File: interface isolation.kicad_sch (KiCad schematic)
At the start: 27 parts, among them J1 Conn_01x09_Socket, J2 Conn_01x02, Q1 Q_NPN_BCE, Q2 Q_NPN_BCE, Q3 Q_NPN_BCE, Q4 Q_NPN_BCE, U1 PC817, U2 PC817, U3 PC817, U4 PC817

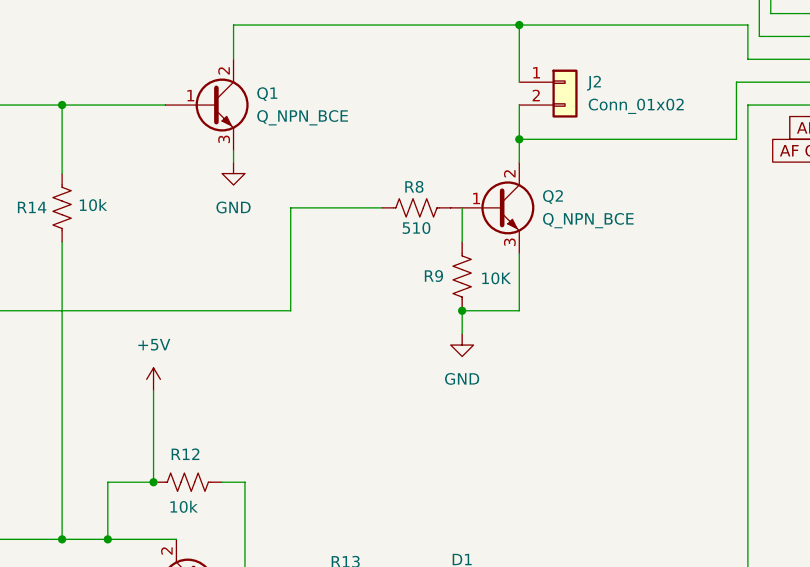
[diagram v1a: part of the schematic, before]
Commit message: Assign footprints to devices
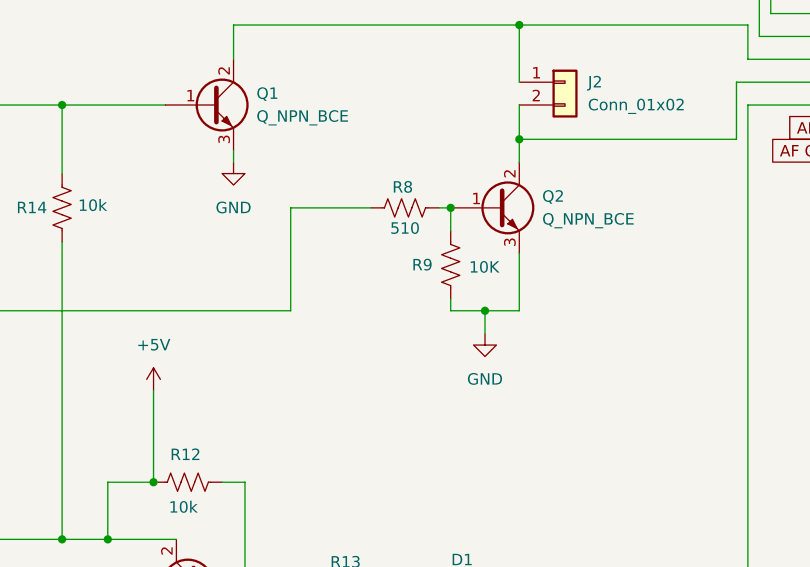
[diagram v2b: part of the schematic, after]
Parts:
- C6: footprint (none) -> Capacitor_SMD:C_0201_0603Metric
- D1, D2: footprint Diode_THT:D_DO-35_SOD27_P7.62mm_Horizontal -> Diode_SMD:D_0603_1608Metric
- J1: footprint (none) -> Connector_Dsub:DSUB-9_Male_EdgeMount_P2.77mm
- J2: footprint (none) -> Connector_PinHeader_1.00mm:PinHeader_1x02_P1.00mm_Vertical
- Q1, Q2, Q3, Q4: footprint (none) -> Package_TO_SOT_SMD:SOT-23-3
- R1, R10, R11, R12, R13, R14, R2, R3, R4, R5, R6, R7, R8, R9: footprint (none) -> Resistor_SMD:R_0201_0603Metric
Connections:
- net at R9.2: now also Q2.1 (B), R8.2
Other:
- moved on the sheet: R8, R9
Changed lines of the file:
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@@
 	)
 	(junction
-		(at 137.16 142.24)
+		(at 171.45 100.33)
 		(diameter 0)
 		(color 0 0 0 0)
 	)
 	(junction
-		(at 168.91 100.33)
+		(at 137.16 142.24)
 		(diameter 0)
 		(color 0 0 0 0)
@@
 	)
 	(junction
+		(at 167.64 88.9)
+		(diameter 0)
+		(color 0 0 0 0)
+	)
+	(junction
 		(at 144.78 130.81)
 		(diameter 0)
@@
 	(wire
 		(pts
-			(xy 149.86 88.9) (xy 160.02 88.9)
+			(xy 149.86 88.9) (xy 158.75 88.9)
 		)
 		(stroke
@@
 	(wire
 		(pts
-			(xy 168.91 100.33) (xy 168.91 102.87)
+			(xy 171.45 100.33) (xy 171.45 102.87)
 		)
 		(stroke
@@
 	(wire
 		(pts
+			(xy 167.64 99.06) (xy 167.64 100.33)
+		)
+		(stroke
+			(width 0)
+			(type default)
+		)
+	)
+	(wire
+		(pts
 			(xy 107.95 52.07) (xy 101.6 52.07)
 		)
@@
 	(wire
 		(pts
+			(xy 167.64 100.33) (xy 171.45 100.33)
+		)
+		(stroke
+			(width 0)
+			(type default)
+		)
+	)
+	(wire
+		(pts
 			(xy 199.39 74.93) (xy 213.36 74.93)
 		)
@@
 	(wire
 		(pts
-			(xy 175.26 100.33) (xy 168.91 100.33)
+			(xy 175.26 100.33) (xy 171.45 100.33)
 		)
 		(stroke
@@
 	(wire
 		(pts
+			(xy 166.37 88.9) (xy 167.64 88.9)
+		)
+		(stroke
+			(width 0)
+			(type default)
+		)
+	)
+	(wire
+		(pts
 			(xy 105.41 147.32) (xy 105.41 152.4)
 		)
@@
 	(wire
 		(pts
-			(xy 168.91 88.9) (xy 168.91 92.71)
+			(xy 167.64 88.9) (xy 167.64 91.44)
 		)
 		(stroke
@@
 	(symbol
 		(lib_id "Device:R_US")
-		(at 168.91 96.52 180)
+		(at 167.64 95.25 180)
 		(unit 1)
 		(exclude_from_sim no)
@@
 		(dnp no)
 		(property "Reference" "R9"
-			(at 164.592 96.52 0)
+			(at 163.322 95.25 0)
 			(effects
 				(font
@@
 		)
 		(property "Value" "10K"
-			(at 170.942 96.774 0)
+			(at 169.672 95.504 0)
 			(effects
 				(font
@@
 			)
 		)
-		(property "Footprint" ""
-			(at 167.894 96.266 90)
+		(property "Footprint" "Resistor_SMD:R_0201_0603Metric"
+			(at 166.624 94.996 90)
 			(effects
 				(font
@@
 		)
 		(property "Datasheet" "~"
-			(at 168.91 96.52 0)
+			(at 167.64 95.25 0)
 			(effects
 				(font
@@
 		)
 		(property "Description" "Resistor, US symbol"
-			(at 168.91 96.52 0)
+			(at 167.64 95.25 0)
 			(effects
 				(font
@@
 			)
 		)
-		(property "Footprint" ""
+		(property "Footprint" "Resistor_SMD:R_0201_0603Metric"
 			(at 123.444 88.646 90)
 			(effects
@@
 	(symbol
 		(lib_id "Device:R_US")
-		(at 163.83 88.9 90)
+		(at 162.56 88.9 90)
 		(unit 1)
 		(exclude_from_sim no)
@@
 		(dnp no)
 		(property "Reference" "R8"
-			(at 163.576 86.614 90)
+			(at 162.306 86.614 90)
 			(effects
 				(font
@@
 		)
 		(property "Value" "510"
-			(at 163.83 91.186 90)
+			(at 162.56 91.186 90)
 			(effects
 				(font
@@
 			)
 		)
-		(property "Footprint" ""
-			(at 164.084 87.884 90)
+		(property "Footprint" "Resistor_SMD:R_0201_0603Metric"
+			(at 162.814 87.884 90)
 			(effects
 				(font
@@
 		)
 		(property "Datasheet" "~"
-			(at 163.83 88.9 0)
+			(at 162.56 88.9 0)
 			(effects
 				(font
@@
 		)
 		(property "Description" "Resistor, US symbol"
-			(at 163.83 88.9 0)
+			(at 162.56 88.9 0)
 			(effects
 				(font
@@
 			)
 		)
-		(property "Footprint" ""
+		(property "Footprint" "Connector_Dsub:DSUB-9_Male_EdgeMount_P2.77mm"
 			(at 218.44 77.47 0)
 			(effects
@@
 			)
 		)
-		(property "Footprint" ""
+		(property "Footprint" "Resistor_SMD:R_0201_0603Metric"
 			(at 75.184 76.454 90)
 			(effects
@@
 			)
 		)
-		(property "Footprint" ""
+		(property "Footprint" "Resistor_SMD:R_0201_0603Metric"
 			(at 171.704 51.054 90)
 			(effects
@@
 			)
 		)
-		(property "Footprint" ""
+		(property "Footprint" "Resistor_SMD:R_0201_0603Metric"
 			(at 136.144 145.796 90)
 			(effects
@@
 			)
 		)
-		(property "Footprint" ""
+		(property "Footprint" "Resistor_SMD:R_0201_0603Metric"
 			(at 138.684 118.364 90)
 			(effects
@@
 			)
 		)
-		(property "Footprint" ""
+		(property "Footprint" "Resistor_SMD:R_0201_0603Metric"
 			(at 106.934 64.516 90)
 			(effects
@@
 			)
 		)
-		(property "Footprint" ""
+		(property "Footprint" "Resistor_SMD:R_0201_0603Metric"
 			(at 156.464 129.794 90)
 			(effects
@@
 			)
 		)
-		(property "Footprint" ""
+		(property "Footprint" "Connector_PinHeader_1.00mm:PinHeader_1x02_P1.00mm_Vertical"
 			(at 180.34 74.93 0)
 			(effects
@@
 			)
 		)
-		(property "Footprint" "Diode_THT:D_DO-35_SOD27_P7.62mm_Horizontal"
+		(property "Footprint" "Diode_SMD:D_0603_1608Metric"
 			(at 168.91 130.81 0)
 			(effects
@@
 			)
 		)
-		(property "Footprint" ""
+		(property "Footprint" "Capacitor_SMD:C_0201_0603Metric"
 			(at 117.8052 139.7 0)
 			(effects
@@
 			)
 		)
-		(property "Footprint" ""
+		(property "Footprint" "Package_TO_SOT_SMD:SOT-23-3"
 			(at 177.8 86.36 0)
 			(effects
@@
 			)
 		)
-		(property "Footprint" ""
+		(property "Footprint" "Resistor_SMD:R_0201_0603Metric"
 			(at 73.914 99.314 90)
 			(effects
@@
 			)
 		)
-		(property "Footprint" ""
+		(property "Footprint" "Package_TO_SOT_SMD:SOT-23-3"
 			(at 134.62 128.27 0)
 			(effects
@@
 			)
 		)
-		(property "Footprint" ""
+		(property "Footprint" "Resistor_SMD:R_0201_0603Metric"
 			(at 72.136 138.684 90)
 			(effects
@@
 			)
 		)
-		(property "Footprint" ""
+		(property "Footprint" "Package_TO_SOT_SMD:SOT-23-3"
 			(at 146.05 74.93 0)
 			(effects
@@
 			)
 		)
-		(property "Footprint" ""
+		(property "Footprint" "Resistor_SMD:R_0201_0603Metric"
 			(at 152.654 54.864 90)
 			(effects
@@
 	(symbol
 		(lib_id "power:GND")
-		(at 168.91 102.87 0)
+		(at 171.45 102.87 0)
 		(unit 1)
 		(exclude_from_sim no)
@@
 		(fields_autoplaced yes)
 		(property "Reference" "#PWR020"
-			(at 168.91 109.22 0)
+			(at 171.45 109.22 0)
 			(effects
 				(font
@@
 		)
 		(property "Value" "GND"
-			(at 168.91 107.95 0)
+			(at 171.45 107.95 0)
 			(effects
 				(font
@@
 		)
 		(property "Footprint" ""
-			(at 168.91 102.87 0)
+			(at 171.45 102.87 0)
 			(effects
 				(font
@@
 		)
 		(property "Datasheet" ""
-			(at 168.91 102.87 0)
+			(at 171.45 102.87 0)
 			(effects
 				(font
@@
 		)
 		(property "Description" "Power symbol creates a global label with name \"GND\" , ground"
-			(at 168.91 102.87 0)
+			(at 171.45 102.87 0)
 			(effects
 				(font
@@
 			)
 		)
-		(property "Footprint" ""
+		(property "Footprint" "Resistor_SMD:R_0201_0603Metric"
 			(at 105.664 141.224 90)
 			(effects
@@
 			)
 		)
-		(property "Footprint" ""
+		(property "Footprint" "Resistor_SMD:R_0201_0603Metric"
 			(at 70.866 48.514 90)
 			(effects
@@
 			)
 		)
-		(property "Footprint" "Diode_THT:D_DO-35_SOD27_P7.62mm_Horizontal"
+		(property "Footprint" "Diode_SMD:D_0603_1608Metric"
 			(at 171.45 43.18 0)
 			(effects
@@
 			)
 		)
-		(property "Footprint" ""
+		(property "Footprint" "Package_TO_SOT_SMD:SOT-23-3"
 			(at 139.7 48.26 0)
 			(effects

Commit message: Place Audio tranformers and cleanup routing.    Re-annotate based on geographical layout.
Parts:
- J1: footprint Connector_Dsub:DSUB-9_Male_EdgeMount_P2.77mm -> Connector_Dsub:DSUB-9_Female_Horizontal_P2.77x2.84mm_EdgePinOffset4.94mm_Housed_MountingHolesOffset7.48mm
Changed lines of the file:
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@@
 			)
 		)
-		(property "Footprint" "Connector_Dsub:DSUB-9_Male_EdgeMount_P2.77mm"
+		(property "Footprint" "Connector_Dsub:DSUB-9_Female_Horizontal_P2.77x2.84mm_EdgePinOffset4.94mm_Housed_MountingHolesOffset7.48mm"
 			(at 218.44 77.47 0)
 			(effects

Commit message: Move Radio interface onto it's own sheet, Add mounting holes and case outline
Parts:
- removed J1: Conn_01x09_Socket, Connector_Dsub:DSUB-9_Female_Horizontal_P2.77x2.84mm_EdgePinOffset4.94mm_Housed_MountingHolesOffset7.48mm, symbol Connector:Conn_01x09_Socket
- renumbered C6 to C12, D1 to D4, D2 to D5, Q4 to Q1, Q3 to Q2, Q2 to Q3, Q1 to Q4, R1 to R11, R5 to R12, R12 to R13, R13 to R14, R9 to R15, R6 to R16, R7 to R17, R8 to R18, R10 to R19, R14 to R20, R3 to R6, R4 to R8, R11 to R9, U4 to U5, U2 to U6, U3 to U7, U1 to U8
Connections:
- net ~COS: now reaches D5.1 (K)
- net COS: now reaches R16.2
- net PTT: now reaches J2.1 (Pin_1), Q4.2 (C)
- net CAT RX: now reaches J2.2 (Pin_2), Q3.2 (C)
- net CAT TX: now reaches D4.1 (K)
